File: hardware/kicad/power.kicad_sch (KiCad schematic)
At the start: 14 parts, among them J101 Superseal 1.5 6p (cablaggio), J102 Superseal 1.5 4p (cablaggio), J103 5V al Pi Zero 2 W, Q101 IRF4905, U101 Pololu D36V28F5

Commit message: Translate code, hardware and docs to English; bilingual dashboard
- tdm-logic i18n module: every dashboard text in English and Italian,
  chosen by `[display] language` in the profile (English by default, the
  TDM 850 profile keeps Italian); number formatting per language
- Slint fixed labels moved to a `Labels` global filled from the same table;
  `tdm-dash --language en|it`; reference screens regenerated in English with
  Italian check screens
- tdmctl, tdm-dash CLI, simulator scenarios, calibration errors and tools
  print English
- KiCad sheets, WireViz harnesses, perfboard plan and CAD comments in
  English, exports regenerated with the new names
- manual, research, ADRs and READMEs translated; files renamed (docs/manual,
  docs/research, English chapter and ADR names); status markers are now
  [VERIFIED] / [TO VERIFY] / [HYPOTHESIS]

Co-Authored-By: Claude Opus 5.5 <noreply@anthropic.com>
Claude-Session: https://claude.ai/code/session_01G9D4Wshjz9MkaThp4wsrGP
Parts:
- J101: value Superseal 1.5 6p (cablaggio) -> Superseal 1.5 6p (harness)
- J102: value Superseal 1.5 4p (cablaggio) -> Superseal 1.5 4p (harness)
- J103: value 5V al Pi Zero 2 W -> 5V to Pi Zero 2 W
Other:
- note added: "+12V_KEY: switched +12 V from the bike harness (Br wire [TO VERIFY]). Chain: 2 A fuse → reverse-polarity P-MOSFET → TVS → LC filter → 5 V buck. The Pico is supplied through D103 with 470 µF of hold-up, to save the km when the key goes off."
- note added: "5 V 3.2 A buck module, input up to 50 V. 1 VIN · 2 GND · 3 VOUT · 4 EN · 5 PG"
- note added: "Power supply and protection"
- note removed: "+12V_KEY: +12 V sotto chiave dal cablaggio della moto (filo Br [DA VERIFICARE]). Catena: fusibile 2 A → P-MOSFET contro l'inversione → TVS → filtro LC → buck 5 V. Il Pico è alimentato attraverso D103 con 470 µF di riserva per salvare i km a chiave tolta."
- note removed: "Alimentazione e protezioni"
- note removed: "Modulo buck 5 V 3,2 A, ingresso fino a 50 V. 1 VIN · 2 GND · 3 VOUT · 4 EN · 5 PG"
- title: Alimentazione e protezioni -> Power supply and protection
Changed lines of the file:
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@@
 	(paper "A4")
 	(title_block
-		(title "Alimentazione e protezioni")
+		(title "Power supply and protection")
 		(date "2026-10-21")
 		(rev "0.1")
 		(company "tdm-dash · CERN-OHL-P-2.0")
-		(comment 1 "Foglio 1 di 8")
-		(comment 2 "Generato da hardware/kicad/generate.py: non modificare a mano")
+		(comment 1 "Sheet 1 of 8")
+		(comment 2 "Generated by hardware/kicad/generate.py: do not edit by hand")
 	)
 	(symbol
@@
 			)
 		)
-		(property "Value" "Superseal 1.5 6p (cablaggio)"
+		(property "Value" "Superseal 1.5 6p (harness)"
 			(at 25.4 73.66 0)
 			(effects
@@
 			)
 		)
-		(property "Value" "Superseal 1.5 4p (cablaggio)"
+		(property "Value" "Superseal 1.5 4p (harness)"
 			(at 25.4 109.22 0)
 			(effects
@@
 			)
 		)
-		(property "Value" "5V al Pi Zero 2 W"
+		(property "Value" "5V to Pi Zero 2 W"
 			(at 246.634 114.3 0)
 			(effects
@@
 		)
 	)
-	(text "Alimentazione e protezioni"
+	(text "Power supply and protection"
 		(exclude_from_sim no)
 		(at 10.16 12.7 0)
@@
 		)
 	)
-	(text "+12V_KEY: +12 V sotto chiave dal cablaggio della moto (filo Br [DA VERIFICARE]).\nCatena: fusibile 2 A → P-MOSFET contro l'inversione → TVS → filtro LC → buck 5 V.\nIl Pico è alimentato attraverso D103 con 470 µF di riserva per salvare i km a chiave tolta."
+	(text "+12V_KEY: switched +12 V from the bike harness (Br wire [TO VERIFY]).\nChain: 2 A fuse → reverse-polarity P-MOSFET → TVS → LC filter → 5 V buck.\nThe Pico is supplied through D103 with 470 µF of hold-up, to save the km when the key goes off."
 		(exclude_from_sim no)
 		(at 10.16 17.78 0)
@@
 		)
 	)
-	(text "Modulo buck 5 V 3,2 A, ingresso fino a 50 V.\n1 VIN · 2 GND · 3 VOUT · 4 EN · 5 PG"
+	(text "5 V 3.2 A buck module, input up to 50 V.\n1 VIN · 2 GND · 3 VOUT · 4 EN · 5 PG"
 		(exclude_from_sim no)
 		(at 226.06 71.12 0)

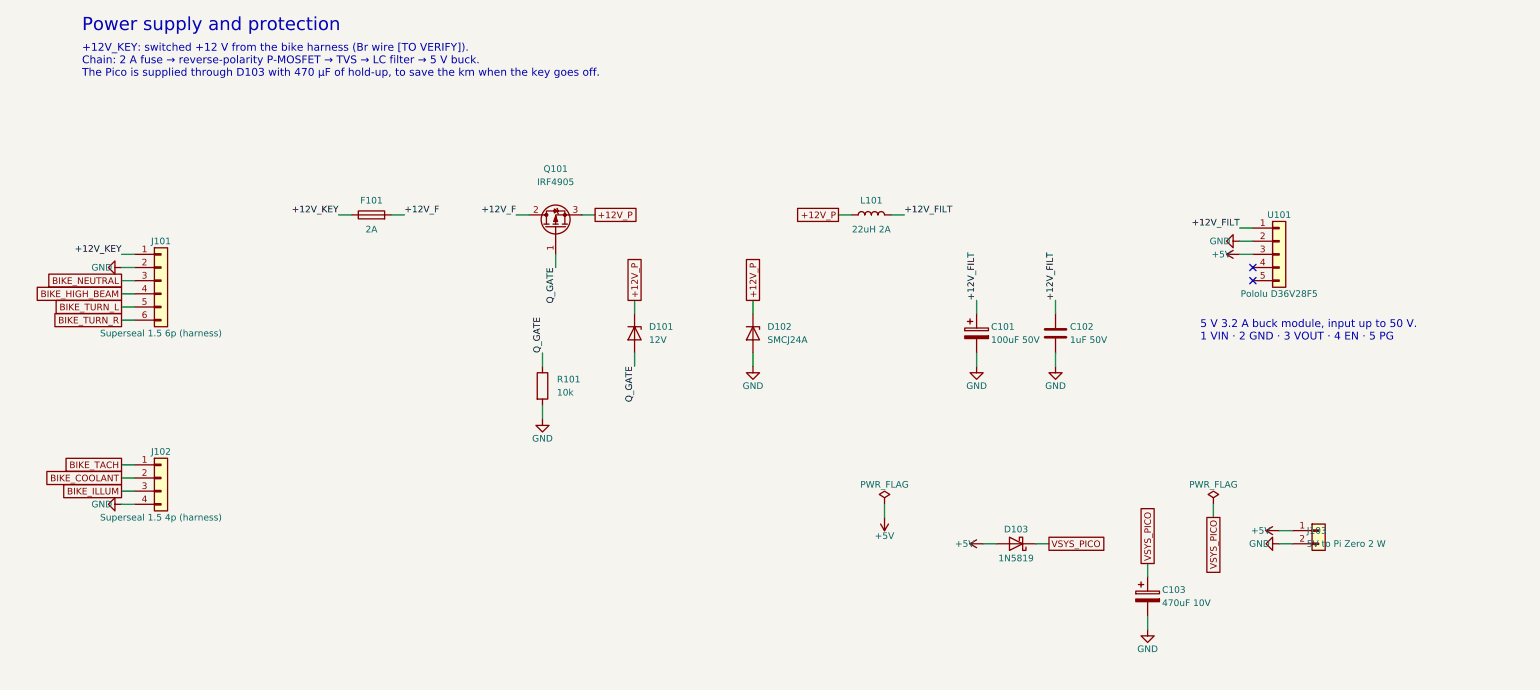
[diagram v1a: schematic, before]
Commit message: Schematic: drawn wires, block diagram, new title block
The sheets were a netlist in disguise: every pin ended in a short stub and
a label, so the circuits had to be pieced together by name, labels
overlapped, two sheets fell off the index page and the title block was
KiCad's default. The generator now draws the schematic:

- hardware/kicad/schgen: placement on the 50 mil grid, orthogonal wires,
  junctions, hierarchical ports, module and connector symbols with named
  pins; the drawing is normalised the way KiCad 9 reads it and checked
  against the declared netlist (no wire may connect anything else)
- hardware/kicad/sheets: one module per sheet, laid out left to right
  from the bike to the Pico; the root sheet is a block diagram whose
  wires are the signals between sheets
- tdm-dash.kicad_wks: frame and title block of the project
- symbols copied from KiCad 9.0.9 (vendor_symbols.py): the generator no
  longer needs KiCad installed
- export.sh: ERC, tools/check_netlist.py (KiCad's netlist is the declared
  one), check_pinmap.py, PDF and SVG on white, tools/check_svg_layout.py
  (no text over another text, a wire, the frame or the title block)

The circuit is unchanged: KiCad's netlist of the old and new schematic
has the same 56 nets (FRAM pins now follow the breakout header, R603/R604
pins swapped).

Co-Authored-By: Claude Opus 5.5 <noreply@anthropic.com>
Claude-Session: https://claude.ai/code/session_01G9D4Wshjz9MkaThp4wsrGP
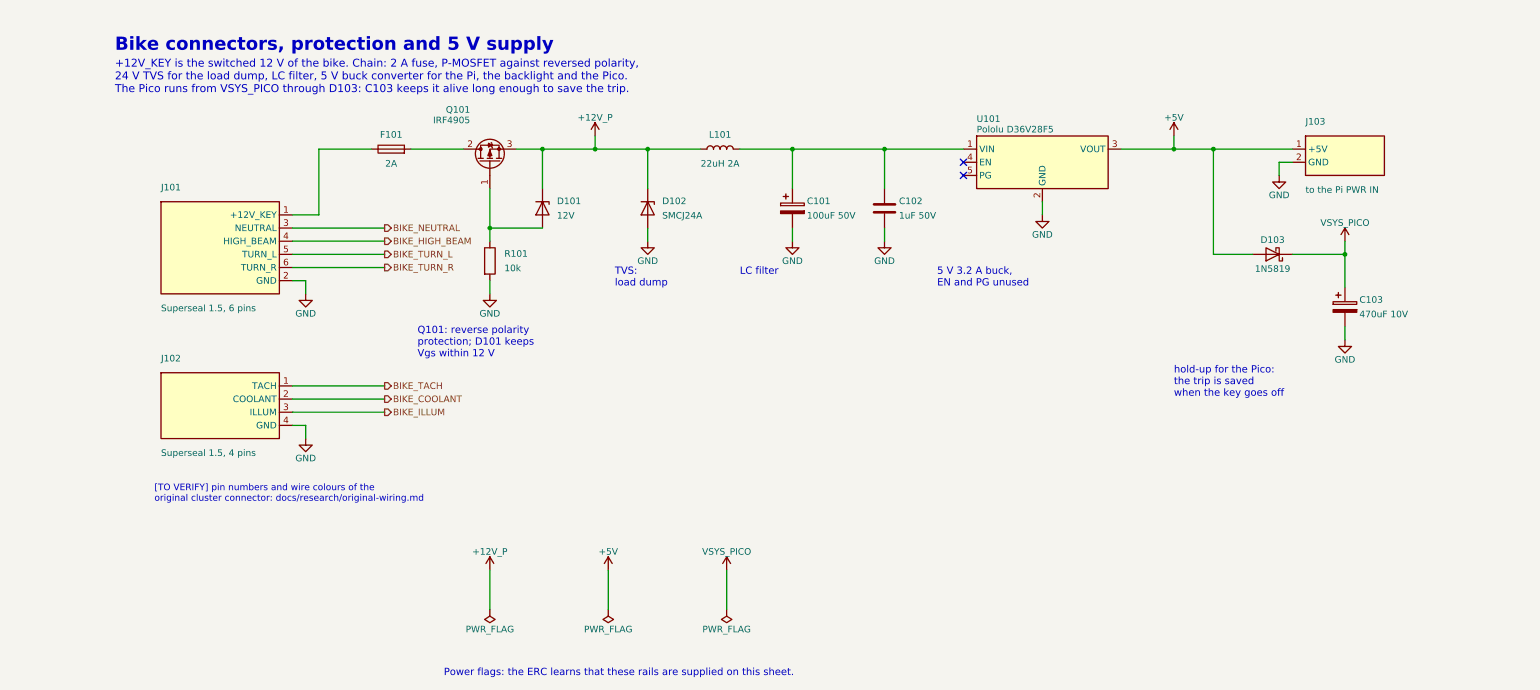
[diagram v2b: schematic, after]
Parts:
- removed J101: Superseal 1.5 6p (harness), symbol Connector_Generic:Conn_01x06
- removed J102: Superseal 1.5 4p (harness), symbol Connector_Generic:Conn_01x04
- removed J103: 5V to Pi Zero 2 W, symbol Connector_Generic:Conn_01x02
- removed U101: Pololu D36V28F5, symbol Connector_Generic:Conn_01x05
- added J101: Superseal 1.5, 6 pins, symbol tdm:Conn_Bike6
- added J102: Superseal 1.5, 4 pins, symbol tdm:Conn_Bike4
- added J103: to the Pi PWR IN, symbol tdm:Conn_Pi5V
- added U101: Pololu D36V28F5, symbol tdm:D36V28F5
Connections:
- net +5V: now also J103.1 (+5V), U101.3 (VOUT)
- net BIKE_COOLANT: now also J102.2 (COOLANT)
- net BIKE_HIGH_BEAM: now also J101.4 (HIGH_BEAM)
- net BIKE_ILLUM: now also J102.3 (ILLUM)
- net BIKE_NEUTRAL: now also J101.3 (NEUTRAL)
- net BIKE_TACH: now also J102.1 (TACH)
- net BIKE_TURN_L: now also J101.5 (TURN_L)
- net BIKE_TURN_R: now also J101.6 (TURN_R)
- net GND: now also J101.2 (GND), J102.4 (GND), J103.2 (GND), U101.2 (GND)
- net +12V_F: no longer names the net of F101.2, Q101.2 (D)
- net +12V_FILT: no longer names the net of C101.1, C102.1, L101.2
- net +12V_FILT: now also U101.1 (VIN)
- net +12V_KEY: no longer names the net of F101.1
- net +12V_KEY: now also J101.1 (+12V_KEY)
- net Q_GATE: no longer names the net of D101.2 (A), Q101.1 (G), R101.1
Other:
- note added: "+12V_KEY is the switched 12 V of the bike. Chain: 2 A fuse, P-MOSFET against reversed polarity, 24 V TVS for the load dump, LC filter, 5 V buck converter for the Pi, the backlight and the Pico. The Pico runs from VSYS_PICO through D103: C103 keeps it alive long enough to save the trip."
- note added: "5 V 3.2 A buck, EN and PG unused"
- note added: "Bike connectors, protection and 5 V supply"
- note added: "LC filter"
- note added: "Power flags: the ERC learns that these rails are supplied on this sheet."
- note added: "Q101: reverse polarity protection; D101 keeps Vgs within 12 V"
- note added: "TVS: load dump"
- note added: "[TO VERIFY] pin numbers and wire colours of the original cluster connector: docs/research/original-wiring.md"
- note added: "hold-up for the Pico: the trip is saved when the key goes off"
- note removed: "+12V_KEY: switched +12 V from the bike harness (Br wire [TO VERIFY]). Chain: 2 A fuse → reverse-polarity P-MOSFET → TVS → LC filter → 5 V buck. The Pico is supplied through D103 with 470 µF of hold-up, to save the km when the key goes off."
- note removed: "5 V 3.2 A buck module, input up to 50 V. 1 VIN · 2 GND · 3 VOUT · 4 EN · 5 PG"
- note removed: "Power supply and protection"
- company: tdm-dash · CERN-OHL-P-2.0 -> tdm-dash

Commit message: Schematic: backlight breakout off the board, harness fuse, micro-USB plug
The perfboard has no room for the TPS61169 breakout, and the build steps
already wired it off the board: J701 now gives it +5 V, CTRL and ground,
and its output goes to the panel LED pins (J704), in a dashed box like the
buttons. F101 is marked as the inline fuse of the adapter harness, J401 as
the terminal for the sensor cable, and J703 has the five pins of the
micro-USB plug, with ID tied to ground.

Co-Authored-By: Claude Opus 5.5 <noreply@anthropic.com>
Claude-Session: https://claude.ai/code/session_01G9D4Wshjz9MkaThp4wsrGP
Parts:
- F101: value 2A -> 2A, in the harness
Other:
- note added: "+12V_KEY is the switched 12 V of the bike. Chain: 2 A fuse in the harness, P-MOSFET against reversed polarity, 24 V TVS for the load dump, LC filter, 5 V buck converter for the Pi, the backlight and the Pico. The Pico runs from VSYS_PICO through D103: C103 keeps it alive long enough to save the trip."
- note added: "[TO VERIFY] pin numbers and wire colors of the original cluster connector: docs/research/original-wiring.md"
- note removed: "+12V_KEY is the switched 12 V of the bike. Chain: 2 A fuse, P-MOSFET against reversed polarity, 24 V TVS for the load dump, LC filter, 5 V buck converter for the Pi, the backlight and the Pico. The Pico runs from VSYS_PICO through D103: C103 keeps it alive long enough to save the trip."
- note removed: "[TO VERIFY] pin numbers and wire colours of the original cluster connector: docs/research/original-wiring.md"
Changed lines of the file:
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@@
 		)
 	)
-	(text "+12V_KEY is the switched 12 V of the bike. Chain: 2 A fuse, P-MOSFET against reversed polarity,\n24 V TVS for the load dump, LC filter, 5 V buck converter for the Pi, the backlight and the Pico.\nThe Pico runs from VSYS_PICO through D103: C103 keeps it alive long enough to save the trip."
+	(text "+12V_KEY is the switched 12 V of the bike. Chain: 2 A fuse in the harness, P-MOSFET against reversed\npolarity, 24 V TVS for the load dump, LC filter, 5 V buck converter for the Pi, the backlight and the Pico.\nThe Pico runs from VSYS_PICO through D103: C103 keeps it alive long enough to save the trip."
 		(exclude_from_sim no)
 		(at 16.51 20.828 0)
@@
 		)
 	)
-	(text "[TO VERIFY] pin numbers and wire colours of the\noriginal cluster connector: docs/research/original-wiring.md"
+	(text "[TO VERIFY] pin numbers and wire colors of the\noriginal cluster connector: docs/research/original-wiring.md"
 		(exclude_from_sim no)
 		(at 24.13 102.87 0)
@@
 			)
 		)
-		(property "Value" "2A"
+		(property "Value" "2A, in the harness"
 			(at 69.85 40.894 90)
 			(effects
